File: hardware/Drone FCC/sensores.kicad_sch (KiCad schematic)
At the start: 30 parts, among them J201 Mag Dupont, J202 Mag DF13, J203 GPS Dupont, J204 GPS M8N - DF13, U201 ICM-42688-V, U202 ILPS22QSTR

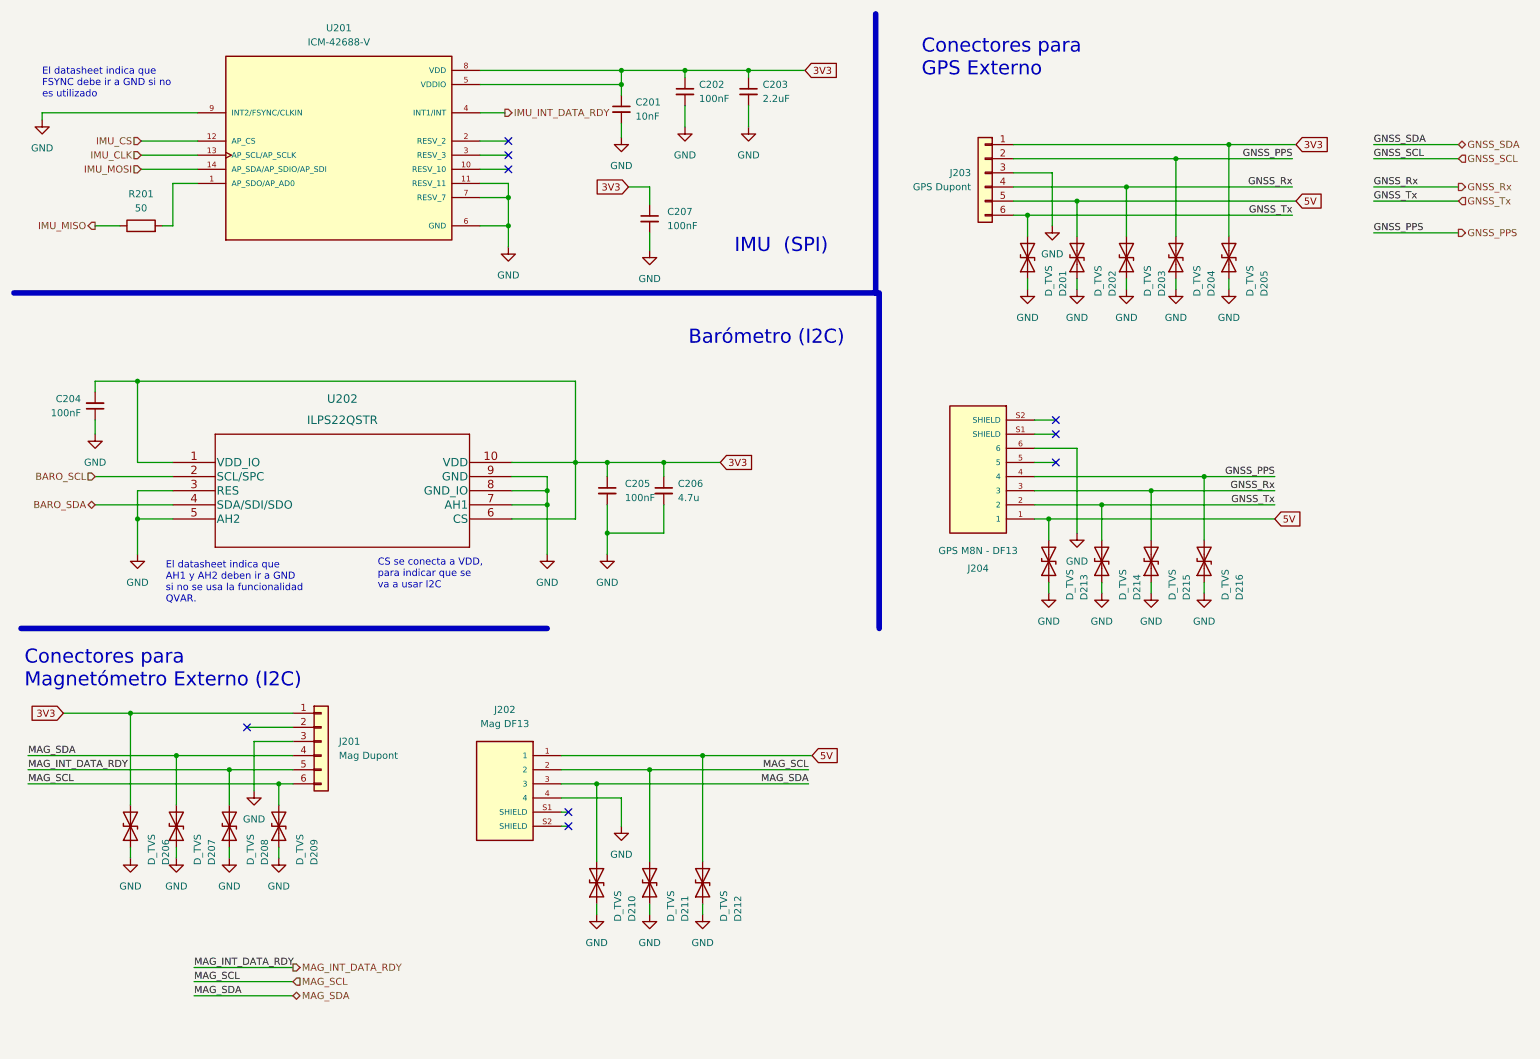
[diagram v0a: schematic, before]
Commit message: removed all the TVS from the PCB and SCH
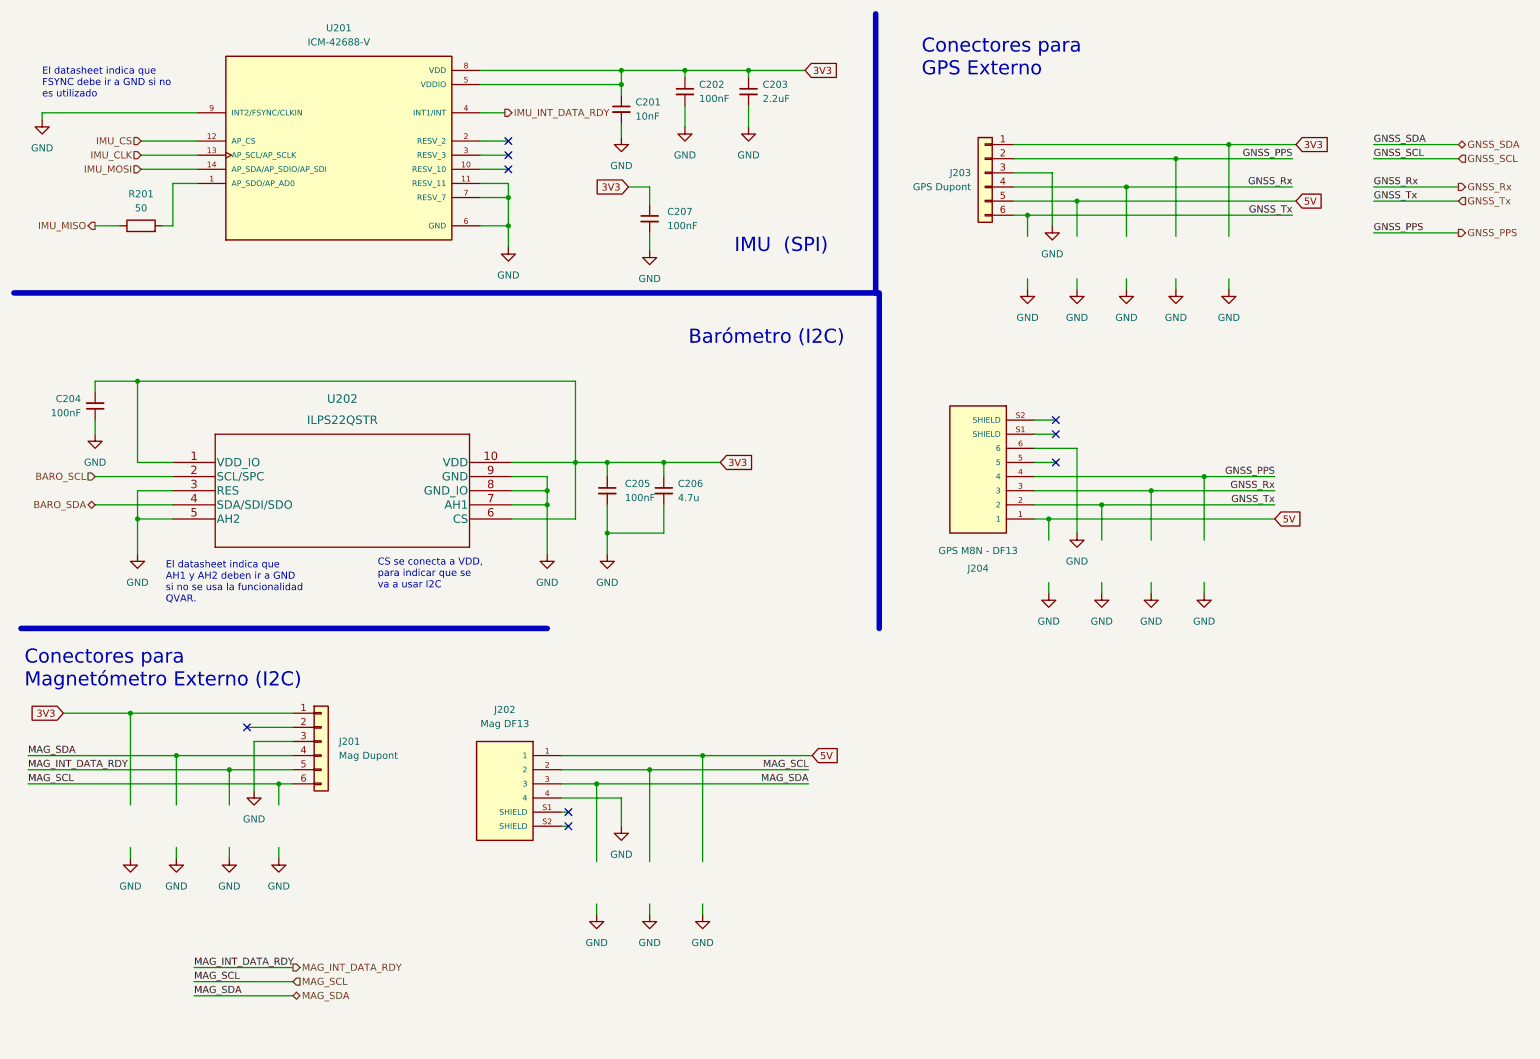
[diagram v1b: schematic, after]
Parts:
- removed D201, D202, D203, D204, D205, D206, D207, D208, D209, D210, D211, D212, D213, D214, D215, D216: D_TVS, Diode_SMD:D_0402_1005Metric_Pad0.77x0.64mm_HandSolder, symbol Device:D_TVS

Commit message: re routed everything with newer dimensions
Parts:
- removed C207: 100nF, Capacitor_SMD:C_0402_1005Metric_Pad0.74x0.62mm_HandSolder, symbol Device:C_Small
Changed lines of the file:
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@@
   (no_connect (at 100.965 37.465))
   (no_connect (at 199.39 87.63))
-  (wire (pts (xy 122.555 43.18) (xy 126.365 43.18))
-    (stroke (width 0) (type default) (color 0 0 0 0))
-  )
   (wire (pts (xy 121.285 22.225) (xy 132.715 22.225))
     (stroke (width 0) (type default) (color 0 0 0 0))
@@
     (stroke (width 0) (type default) (color 0 0 0 0))
   )
-  (wire (pts (xy 126.365 43.18) (xy 126.365 46.355))
-    (stroke (width 0) (type default) (color 0 0 0 0))
-  )
-  (wire (pts (xy 126.365 51.435) (xy 126.365 54.61))
-    (stroke (width 0) (type default) (color 0 0 0 0))
-  )
   (wire (pts (xy 26.67 50.165) (xy 31.115 50.165))
     (stroke (width 0) (type default) (color 0 0 0 0))
@@
     (property "Intersheet References" "${INTERSHEET_REFS}" (id 0) (at 160.2257 22.1456 0)
       (effects (font (size 1.27 1.27)) (justify left) hide)
-    )
-  )
-  (global_label "3V3" (shape input) (at 122.555 43.18 180) (fields_autoplaced)
-    (effects (font (size 1.27 1.27)) (justify right))
-    (property "Intersheet References" "${INTERSHEET_REFS}" (id 0) (at 116.6343 43.2594 0)
-      (effects (font (size 1.27 1.27)) (justify right) hide)
     )
   )
@@
     (pin "5")
     (pin "6")
-  )
-  (symbol (lib_id "Device:C_Small") (at 126.365 48.895 0) (unit 1)
-    (in_bom yes) (on_board yes) (fields_autoplaced)
-    (property "Reference" "C207" (id 0) (at 129.54 47.6312 0)
-      (effects (font (size 1.27 1.27)) (justify left))
-    )
-    (property "Value" "100nF" (id 1) (at 129.54 50.1712 0)
-      (effects (font (size 1.27 1.27)) (justify left))
-    )
-    (property "Footprint" "Capacitor_SMD:C_0402_1005Metric_Pad0.74x0.62mm_HandSolder" (id 2) (at 126.365 48.895 0)
-      (effects (font (size 1.27 1.27)) hide)
-    )
-    (property "Datasheet" "~" (id 3) (at 126.365 48.895 0)
-      (effects (font (size 1.27 1.27)) hide)
-    )
-    (pin "1")
-    (pin "2")
   )
   (symbol (lib_id "power:GND") (at 220.98 61.595 0) (mirror y) (unit 1)
@@
       (effects (font (size 1.27 1.27)) hide)
     )
-    (pin "1")
-  )
-  (symbol (lib_id "power:GND") (at 126.365 54.61 0) (unit 1)
-    (in_bom yes) (on_board yes) (fields_autoplaced)
-    (property "Reference" "#PWR0145" (id 0) (at 126.365 60.96 0)
-      (effects (font (size 1.27 1.27)) hide)
-    )
-    (property "Value" "GND" (id 1) (at 126.365 59.69 0))
-    (property "Footprint" "" (id 2) (at 126.365 54.61 0)
-      (effects (font (size 1.27 1.27)) hide)
-    )
-    (property "Datasheet" "" (id 3) (at 126.365 54.61 0)
-      (effects (font (size 1.27 1.27)) hide)
-    )

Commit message: re enumeation of componentes
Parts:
- renumbered C204 to C15, C205 to C16, C201 to C17, C206 to C18, C202 to C19, C203 to C20, J201 to J20, J202 to J21, J204 to J22, J203 to J23, R201 to R11, U202 to U4, U201 to U5
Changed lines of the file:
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@@
   (symbol (lib_id "power:GND") (at 132.715 32.385 0) (unit 1)
     (in_bom yes) (on_board yes) (fields_autoplaced)
-    (property "Reference" "#PWR0105" (id 0) (at 132.715 38.735 0)
+    (property "Reference" "#PWR039" (id 0) (at 132.715 38.735 0)
       (effects (font (size 1.27 1.27)) hide)
     )
@@
   (symbol (lib_id "power:GND") (at 107.95 109.22 0) (unit 1)
     (in_bom yes) (on_board yes) (fields_autoplaced)
-    (property "Reference" "#PWR0113" (id 0) (at 107.95 115.57 0)
+    (property "Reference" "#PWR035" (id 0) (at 107.95 115.57 0)
       (effects (font (size 1.27 1.27)) hide)
     )
@@
   (symbol (lib_id "power:GND") (at 118.745 109.22 0) (unit 1)
     (in_bom yes) (on_board yes) (fields_autoplaced)
-    (property "Reference" "#PWR0109" (id 0) (at 118.745 115.57 0)
+    (property "Reference" "#PWR036" (id 0) (at 118.745 115.57 0)
       (effects (font (size 1.27 1.27)) hide)
     )
@@
   (symbol (lib_id "Device:C_Small") (at 128.905 97.79 0) (unit 1)
     (in_bom yes) (on_board yes) (fields_autoplaced)
-    (property "Reference" "C206" (id 0) (at 131.445 96.5262 0)
+    (property "Reference" "C18" (id 0) (at 131.445 96.5262 0)
       (effects (font (size 1.27 1.27)) (justify left))
     )
@@
   (symbol (lib_id "power:GND") (at 198.755 50.165 0) (mirror y) (unit 1)
     (in_bom yes) (on_board yes)
-    (property "Reference" "#PWR0110" (id 0) (at 198.755 56.515 0)
+    (property "Reference" "#PWR041" (id 0) (at 198.755 56.515 0)
       (effects (font (size 1.27 1.27)) hide)
     )
@@
   (symbol (lib_id "DF13C-69-1.25v(51):DF13C-6P-1.25V(51)") (at 185.42 92.71 180) (unit 1)
     (in_bom yes) (on_board yes)
-    (property "Reference" "J204" (id 0) (at 185.42 111.76 0))
+    (property "Reference" "J22" (id 0) (at 185.42 111.76 0))
     (property "Value" "GPS M8N - DF13" (id 1) (at 185.42 108.585 0))
     (property "Footprint" "DF13C-6P-1.25V(51):HIROSE_DF13C-6P-1.25V(51)" (id 2) (at 185.42 92.71 0)
@@
   (symbol (lib_id "Connector_Generic:Conn_01x06") (at 186.69 40.64 0) (mirror y) (unit 1)
     (in_bom yes) (on_board yes) (fields_autoplaced)
-    (property "Reference" "J203" (id 0) (at 184.15 40.6399 0)
+    (property "Reference" "J23" (id 0) (at 184.15 40.6399 0)
       (effects (font (size 1.27 1.27)) (justify left))
     )
@@
   (symbol (lib_id "ICM-42688-V:ICM-42688-V") (at 70.485 34.925 0) (unit 1)
     (in_bom yes) (on_board yes) (fields_autoplaced)
-    (property "Reference" "U201" (id 0) (at 70.485 14.605 0))
+    (property "Reference" "U5" (id 0) (at 70.485 14.605 0))
     (property "Value" "ICM-42688-V" (id 1) (at 70.485 17.145 0))
     (property "Footprint" "ICM-42688-V:PQFN50P300X250X97-14N" (id 2) (at 70.485 34.925 0)
@@
   (symbol (lib_id "ILPS22QSTR:ILPS22QSTR") (at 40.64 92.71 0) (unit 1)
     (in_bom yes) (on_board yes) (fields_autoplaced)
-    (property "Reference" "U202" (id 0) (at 71.12 81.28 0)
+    (property "Reference" "U4" (id 0) (at 71.12 81.28 0)
       (effects (font (size 1.524 1.524)))
     )
@@
   (symbol (lib_id "power:GND") (at 203.2 105.41 0) (unit 1)
     (in_bom yes) (on_board yes) (fields_autoplaced)
-    (property "Reference" "#PWR0108" (id 0) (at 203.2 111.76 0)
+    (property "Reference" "#PWR042" (id 0) (at 203.2 111.76 0)
       (effects (font (size 1.27 1.27)) hide)
     )
@@
   (symbol (lib_id "Device:C_Small") (at 144.145 26.035 0) (unit 1)
     (in_bom yes) (on_board yes) (fields_autoplaced)
-    (property "Reference" "C203" (id 0) (at 146.685 24.7712 0)
+    (property "Reference" "C20" (id 0) (at 146.685 24.7712 0)
       (effects (font (size 1.27 1.27)) (justify left))
     )
@@
   (symbol (lib_id "Device:C_Small") (at 132.715 26.035 0) (unit 1)
     (in_bom yes) (on_board yes) (fields_autoplaced)
-    (property "Reference" "C202" (id 0) (at 135.255 24.7712 0)
+    (property "Reference" "C19" (id 0) (at 135.255 24.7712 0)
       (effects (font (size 1.27 1.27)) (justify left))
     )
@@
   (symbol (lib_id "Connector_Generic:Conn_01x06") (at 67.31 142.875 0) (unit 1)
     (in_bom yes) (on_board yes) (fields_autoplaced)
-    (property "Reference" "J201" (id 0) (at 70.485 142.8749 0)
+    (property "Reference" "J20" (id 0) (at 70.485 142.8749 0)
       (effects (font (size 1.27 1.27)) (justify left))
     )
@@
   (symbol (lib_id "Device:C_Small") (at 26.67 82.55 0) (mirror x) (unit 1)
     (in_bom yes) (on_board yes) (fields_autoplaced)
-    (property "Reference" "C204" (id 0) (at 24.13 81.2735 0)
+    (property "Reference" "C15" (id 0) (at 24.13 81.2735 0)
       (effects (font (size 1.27 1.27)) (justify right))
     )
@@
   (symbol (lib_id "power:GND") (at 55.245 151.765 0) (unit 1)
     (in_bom yes) (on_board yes) (fields_autoplaced)
-    (property "Reference" "#PWR0107" (id 0) (at 55.245 158.115 0)
+    (property "Reference" "#PWR033" (id 0) (at 55.245 158.115 0)
       (effects (font (size 1.27 1.27)) hide)
     )
@@
   (symbol (lib_id "Device:R") (at 34.925 50.165 90) (unit 1)
     (in_bom yes) (on_board yes) (fields_autoplaced)
-    (property "Reference" "R201" (id 0) (at 34.925 44.45 90))
+    (property "Reference" "R11" (id 0) (at 34.925 44.45 90))
     (property "Value" "50" (id 1) (at 34.925 46.99 90))
     (property "Footprint" "Resistor_SMD:R_0402_1005Metric_Pad0.72x0.64mm_HandSolder" (id 2) (at 34.925 51.943 90)
@@
   (symbol (lib_id "Device:C_Small") (at 121.285 29.21 0) (unit 1)
     (in_bom yes) (on_board yes) (fields_autoplaced)
-    (property "Reference" "C201" (id 0) (at 123.825 27.9462 0)
+    (property "Reference" "C17" (id 0) (at 123.825 27.9462 0)
       (effects (font (size 1.27 1.27)) (justify left))
     )
@@
   (symbol (lib_id "power:GND") (at 17.145 31.115 0) (unit 1)
     (in_bom yes) (on_board yes) (fields_autoplaced)
-    (property "Reference" "#PWR0111" (id 0) (at 17.145 37.465 0)
+    (property "Reference" "#PWR030" (id 0) (at 17.145 37.465 0)
       (effects (font (size 1.27 1.27)) hide)
     )
@@
   (symbol (lib_id "power:GND") (at 144.145 32.385 0) (unit 1)
     (in_bom yes) (on_board yes) (fields_autoplaced)
-    (property "Reference" "#PWR0106" (id 0) (at 144.145 38.735 0)
+    (property "Reference" "#PWR040" (id 0) (at 144.145 38.735 0)
       (effects (font (size 1.27 1.27)) hide)
     )
@@
   (symbol (lib_id "power:GND") (at 100.965 53.975 0) (unit 1)
     (in_bom yes) (on_board yes) (fields_autoplaced)
-    (property "Reference" "#PWR0114" (id 0) (at 100.965 60.325 0)
+    (property "Reference" "#PWR034" (id 0) (at 100.965 60.325 0)
       (effects (font (size 1.27 1.27)) hide)
     )
@@
   (symbol (lib_name "DF13C-4P-1.25V(51)_1") (lib_id "DF13C-4P-1.25V(51):DF13C-4P-1.25V(51)") (at 100.33 155.575 0) (mirror y) (unit 1)
     (in_bom yes) (on_board yes) (fields_autoplaced)
-    (property "Reference" "J202" (id 0) (at 100.33 137.16 0))
+    (property "Reference" "J21" (id 0) (at 100.33 137.16 0))
     (property "Value" "Mag DF13" (id 1) (at 100.33 139.7 0))
     (property "Footprint" "Connector_Hirose:Hirose_DF13C_CL535-0404-8-51_1x04-1MP_P1.25mm_Vertical" (id 2) (at 101.6 164.465 0)
@@
   (symbol (lib_id "power:GND") (at 121.285 34.29 0) (unit 1)
     (in_bom yes) (on_board yes) (fields_autoplaced)
-    (property "Reference" "#PWR0115" (id 0) (at 121.285 40.64 0)
+    (property "Reference" "#PWR037" (id 0) (at 121.285 40.64 0)
       (effects (font (size 1.27 1.27)) hide)
     )
@@
   (symbol (lib_id "power:GND") (at 121.285 158.115 0) (unit 1)
     (in_bom yes) (on_board yes) (fields_autoplaced)
-    (property "Reference" "#PWR0116" (id 0) (at 121.285 164.465 0)
+    (property "Reference" "#PWR038" (id 0) (at 121.285 164.465 0)
       (effects (font (size 1.27 1.27)) hide)
     )
@@
   (symbol (lib_id "power:GND") (at 34.29 109.22 0) (unit 1)
     (in_bom yes) (on_board yes) (fields_autoplaced)
-    (property "Reference" "#PWR0112" (id 0) (at 34.29 115.57 0)
+    (property "Reference" "#PWR032" (id 0) (at 34.29 115.57 0)
       (effects (font (size 1.27 1.27)) hide)
     )
@@
   (symbol (lib_id "Device:C_Small") (at 118.745 97.79 0) (unit 1)
     (in_bom yes) (on_board yes) (fields_autoplaced)
-    (property "Reference" "C205" (id 0) (at 121.92 96.5262 0)
+    (property "Reference" "C16" (id 0) (at 121.92 96.5262 0)
       (effects (font (size 1.27 1.27)) (justify left))
     )
@@
   (symbol (lib_id "power:GND") (at 26.67 87.63 0) (unit 1)
     (in_bom yes) (on_board yes) (fields_autoplaced)
-    (property "Reference" "#PWR01" (id 0) (at 26.67 93.98 0)
-      (effects (font (size 1.27 1.27)) hide)
-    )
+    (property "Reference" "#PWR031" (id 0) (at 26.67 93.98 0)
+      (effects (font (size 1.27 1.27)) hide)
+    )

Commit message: moved NRST cap near mcu pin, changed v meas adc pin
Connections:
- net GND: no longer U5.9 (INT2/FSYNC/CLKIN)
- no-connect marks 9 -> 10
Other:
- note removed: "El datasheet indica que FSYNC debe ir a GND si no es utilizado"
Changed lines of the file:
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@@
   (no_connect (at 199.39 92.71))
   (no_connect (at 53.975 140.335))
+  (no_connect (at 17.145 29.845))
   (no_connect (at 100.965 37.465))
   (no_connect (at 199.39 87.63))
@@
     (stroke (width 0) (type default) (color 0 0 0 0))
   )
-  (wire (pts (xy 17.145 29.845) (xy 17.145 31.115))
-    (stroke (width 0) (type default) (color 0 0 0 0))
-  )
   (wire (pts (xy 118.745 100.33) (xy 118.745 105.41))
     (stroke (width 0) (type default) (color 0 0 0 0))
@@
   (text "El datasheet indica que\nAH1 y AH2 deben ir a GND\nsi no se usa la funcionalidad\nQVAR."
     (at 39.37 118.11 0)
-    (effects (font (size 1.27 1.27)) (justify left bottom))
-  )
-  (text "El datasheet indica que \nFSYNC debe ir a GND si no\nes utilizado"
-    (at 17.145 27.305 0)
     (effects (font (size 1.27 1.27)) (justify left bottom))
   )
@@
     (pin "2")
   )
-  (symbol (lib_id "power:GND") (at 17.145 31.115 0) (unit 1)
-    (in_bom yes) (on_board yes) (fields_autoplaced)
-    (property "Reference" "#PWR030" (id 0) (at 17.145 37.465 0)
-      (effects (font (size 1.27 1.27)) hide)
-    )
-    (property "Value" "GND" (id 1) (at 17.145 36.195 0))
-    (property "Footprint" "" (id 2) (at 17.145 31.115 0)
-      (effects (font (size 1.27 1.27)) hide)
-    )
-    (property "Datasheet" "" (id 3) (at 17.145 31.115 0)
-      (effects (font (size 1.27 1.27)) hide)
-    )
-    (pin "1")
-  )
   (symbol (lib_id "power:GND") (at 144.145 32.385 0) (unit 1)

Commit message: updated BOM with passive components
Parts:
- R11: value 50 -> 0
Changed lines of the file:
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@@
     (in_bom yes) (on_board yes) (fields_autoplaced)
     (property "Reference" "R11" (id 0) (at 34.925 44.45 90))
-    (property "Value" "50" (id 1) (at 34.925 46.99 90))
+    (property "Value" "0" (id 1) (at 34.925 46.99 90))
     (property "Footprint" "Resistor_SMD:R_0402_1005Metric_Pad0.72x0.64mm_HandSolder" (id 2) (at 34.925 51.943 90)
       (effects (font (size 1.27 1.27)) hide)
